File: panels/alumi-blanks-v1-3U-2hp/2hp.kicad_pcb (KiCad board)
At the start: 2 copper layers, 9.8 x 128.5 mm, 2 parts

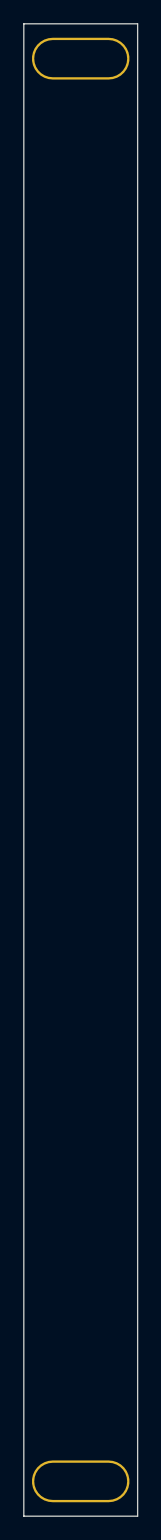
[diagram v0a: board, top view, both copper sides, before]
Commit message: feat: add new screw hole footprints and update panel KiCad files for new JLCPCB order
- Added modular-3M-screw-hole-size1-alumi-0604, modular-3M-screw-hole-size1-fit-alumi-0604, modular-3M-screw-hole-size2-alumi-0604
- Updated all panel .kicad_pcb and .kicad_pro files for 3U panels (1hp-16hp)
- Added new JLCPCB order snapshot and Gerber outputs

Co-authored-by: Copilot <223556219+Copilot@users.noreply.github.com>
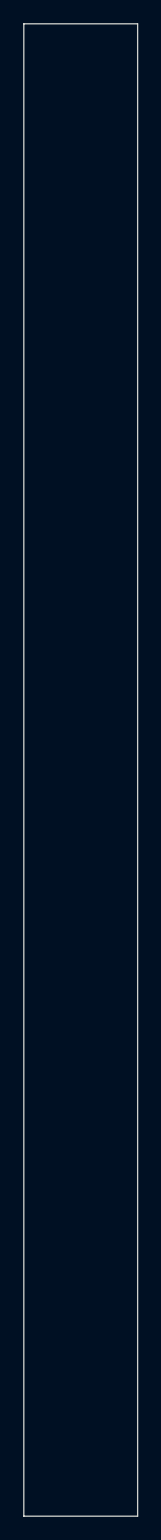
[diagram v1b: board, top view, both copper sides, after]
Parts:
- removed ?: , 
- removed the REF** at (4.90, 125.5)
- added REF**: modular-3M-screw-hole-size1-alumi-0604, zudo-blanks:modular-3M-screw-hole-size1-alumi-0604, F.Cu at (3.50, 3.00)
- added REF**: modular-3M-screw-hole-size1-alumi-0604, zudo-blanks:modular-3M-screw-hole-size1-alumi-0604, F.Cu at (6.29, 125.5)
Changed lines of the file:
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@@
 (kicad_pcb
-	(version 20240108)
+	(version 20260206)
 	(generator "pcbnew")
-	(generator_version "8.0")
+	(generator_version "10.0")
 	(general
 		(thickness 1.6)
@@
 	(layers
 		(0 "F.Cu" signal)
-		(31 "B.Cu" signal)
-		(32 "B.Adhes" user "B.Adhesive")
-		(33 "F.Adhes" user "F.Adhesive")
-		(34 "B.Paste" user)
-		(35 "F.Paste" user)
-		(36 "B.SilkS" user "B.Silkscreen")
-		(37 "F.SilkS" user "F.Silkscreen")
-		(38 "B.Mask" user)
-		(39 "F.Mask" user)
-		(40 "Dwgs.User" user "User.Drawings")
-		(41 "Cmts.User" user "User.Comments")
-		(42 "Eco1.User" user "User.Eco1")
-		(43 "Eco2.User" user "User.Eco2")
-		(44 "Edge.Cuts" user)
-		(45 "Margin" user)
-		(46 "B.CrtYd" user "B.Courtyard")
-		(47 "F.CrtYd" user "F.Courtyard")
-		(48 "B.Fab" user)
-		(49 "F.Fab" user)
-		(50 "User.1" user)
-		(51 "User.2" user)
-		(52 "User.3" user)
-		(53 "User.4" user)
-		(54 "User.5" user)
-		(55 "User.6" user)
-		(56 "User.7" user)
-		(57 "User.8" user)
-		(58 "User.9" user)
+		(2 "B.Cu" signal)
+		(9 "F.Adhes" user "F.Adhesive")
+		(11 "B.Adhes" user "B.Adhesive")
+		(13 "F.Paste" user)
+		(15 "B.Paste" user)
+		(5 "F.SilkS" user "F.Silkscreen")
+		(7 "B.SilkS" user "B.Silkscreen")
+		(1 "F.Mask" user)
+		(3 "B.Mask" user)
+		(17 "Dwgs.User" user "User.Drawings")
+		(19 "Cmts.User" user "User.Comments")
+		(21 "Eco1.User" user "User.Eco1")
+		(23 "Eco2.User" user "User.Eco2")
+		(25 "Edge.Cuts" user)
+		(27 "Margin" user)
+		(31 "F.CrtYd" user "F.Courtyard")
+		(29 "B.CrtYd" user "B.Courtyard")
+		(35 "F.Fab" user)
+		(33 "B.Fab" user)
+		(39 "User.1" user)
+		(41 "User.2" user)
+		(43 "User.3" user)
+		(45 "User.4" user)
+		(47 "User.5" user)
+		(49 "User.6" user)
+		(51 "User.7" user)
+		(53 "User.8" user)
+		(55 "User.9" user)
 	)
 	(setup
 		(pad_to_mask_clearance 0)
 		(allow_soldermask_bridges_in_footprints no)
+		(tenting
+			(front yes)
+			(back yes)
+		)
+		(covering
+			(front no)
+			(back no)
+		)
+		(plugging
+			(front no)
+			(back no)
+		)
+		(capping no)
+		(filling no)
 		(pcbplotparams
-			(layerselection 0x00010fc_ffffffff)
-			(plot_on_all_layers_selection 0x0000000_00000000)
+			(layerselection 0x00000000_00000000_55555555_5755555a)
+			(plot_on_all_layers_selection 0x00000000_00000000_00000000_00000000)
 			(disableapertmacros no)
 			(usegerberextensions no)
@@
 			(usegerberadvancedattributes yes)
 			(creategerberjobfile yes)
-			(dashed_line_dash_ratio 12.000000)
-			(dashed_line_gap_ratio 3.000000)
+			(dashed_line_dash_ratio 12)
+			(dashed_line_gap_ratio 3)
 			(svgprecision 4)
 			(plotframeref no)
-			(viasonmask no)
 			(mode 1)
 			(useauxorigin no)
-			(hpglpennumber 1)
-			(hpglpenspeed 20)
-			(hpglpendiameter 15.000000)
 			(pdf_front_fp_property_popups yes)
 			(pdf_back_fp_property_popups yes)
+			(pdf_metadata yes)
+			(pdf_single_document no)
 			(dxfpolygonmode yes)
 			(dxfimperialunits yes)
@@
 			(psnegative no)
 			(psa4output no)
-			(plotreference yes)
-			(plotvalue yes)
-			(plotfptext yes)
-			(plotinvisibletext no)
+			(plot_black_and_white yes)
 			(sketchpadsonfab no)
+			(plotpadnumbers no)
+			(hidednponfab no)
+			(sketchdnponfab yes)
+			(crossoutdnponfab yes)
 			(subtractmaskfromsilk no)
 			(outputformat 1)
@@
 		)
 	)
-	(net 0 "")
-	(footprint "Takazudo:M3-hole-little-wide-deco"
+	(footprint "zudo-blanks:modular-3M-screw-hole-size1-alumi-0604"
 		(layer "F.Cu")
-		(at 4.9 125.5)
+		(at 3.505 3)
 		(property "Reference" "REF**"
 			(at 0 -0.5 0)
@@
 			)
 		)
-		(property "Value" "M3-hole-little-wide-deco"
+		(property "Value" "modular-3M-screw-hole-size1-alumi-0604"
 			(at 0 1 0)
 			(unlocked yes)
@@
 			)
 		)
-		(property "Footprint" "Takazudo:M3-hole-little-wide-deco"
-			(at 0 0 0)
-			(unlocked yes)
-			(layer "F.Fab")
-			(hide yes)
-			(effects
-				(font
-					(size 1 1)
-					(thickness 0.15)
-				)
-			)
-		)
 		(property "Datasheet" ""
 			(at 0 0 0)
@@
 			)
 		)
-		(attr through_hole)
-		(pad "1" thru_hole roundrect
+		(attr smd)
+		(duplicate_pad_numbers_are_jumpers no)
+		(pad "" np_thru_hole roundrect
 			(at 0 0 90)
-			(size 3.6 8.4)
-			(drill oval 3.2 8)
-			(layers "*.Cu" "*.Mask")
-			(remove_unused_layers no)
-			(roundrect_rratio 0.5)
-		)
-	)
-	(footprint ""
+			(size 4 6)
+			(drill oval 3.2 5.2)
+			(layers "*.Mask")
+			(roundrect_rratio 0.4998750312)
+		)
+		(embedded_fonts no)
+	)
+	(footprint "zudo-blanks:modular-3M-screw-hole-size1-alumi-0604"
 		(layer "F.Cu")
-		(at 4.9 3)
-		(property "Reference" ""
-			(at 0 0 0)
+		(at 6.295 125.5)
+		(property "Reference" "REF**"
+			(at 0 -0.5 0)
+			(unlocked yes)
 			(layer "F.SilkS")
-			(effects
-				(font
-					(size 1.27 1.27)
-					(thickness 0.15)
-				)
-			)
-		)
-		(property "Value" ""
-			(at 0 0 0)
-			(layer "F.Fab")
-			(effects
-				(font
-					(size 1.27 1.27)
-					(thickness 0.15)
-				)
-			)
-		)
-		(property "Footprint" ""
-			(at 0 0 0)
-			(layer "F.Fab")
-			(hide yes)
-			(effects
-				(font
-					(size 1.27 1.27)
+			(hide yes)
+			(effects
+				(font
+					(size 1 1)
+					(thickness 0.1)
+				)
+			)
+		)
+		(property "Value" "modular-3M-screw-hole-size1-alumi-0604"
+			(at 0 1 0)
+			(unlocked yes)
+			(layer "F.Fab")
+			(hide yes)
+			(effects
+				(font
+					(size 1 1)
 					(thickness 0.15)
 				)
@@
 		(property "Datasheet" ""
 			(at 0 0 0)
-			(layer "F.Fab")
-			(hide yes)
-			(effects
-				(font
-					(size 1.27 1.27)
+			(unlocked yes)
+			(layer "F.Fab")
+			(hide yes)
+			(effects
+				(font
+					(size 1 1)
 					(thickness 0.15)
 				)
@@
 		(property "Description" ""
 			(at 0 0 0)
-			(layer "F.Fab")
-			(hide yes)
-			(effects
-				(font
-					(size 1.27 1.27)
-					(thickness 0.15)
-				)
-			)
-		)
-		(pad "1" thru_hole roundrect
+			(unlocked yes)
+			(layer "F.Fab")
+			(hide yes)
+			(effects
+				(font
+					(size 1 1)
+					(thickness 0.15)
+				)
+			)
+		)
+		(attr smd)
+		(duplicate_pad_numbers_are_jumpers no)
+		(pad "" np_thru_hole roundrect
 			(at 0 0 90)
-			(size 3.6 8.4)
-			(drill oval 3.2 8)
-			(layers "*.Cu" "*.Mask")
-			(remove_unused_layers no)
-			(roundrect_rratio 0.5)
-		)
+			(size 4 6)
+			(drill oval 3.2 5.2)
+			(layers "*.Mask")
+			(roundrect_rratio 0.4998750312)
+		)
+		(embedded_fonts no)
 	)
 	(gr_poly
@@
 			(type solid)
 		)
-		(fill solid)
+		(fill yes)
 		(layer "Edge.Cuts")
 	)
 	(gr_poly
 		(pts
+			(xy 0.69944 30.000381) (xy 0.000937 30.000381) (xy 0.000937 -0.000004) (xy 0.69944 -0.000004)
+		)
+		(stroke
+			(width -0.000001)
+			(type solid)
+		)
+		(fill yes)
+		(layer "User.1")
+	)
+	(gr_poly
+		(pts
+			(xy 4.901047 1.199447) (xy 0.000937 1.199447) (xy 0.000937 -0.000004) (xy 4.901047 -0.000004)
+		)
+		(stroke
+			(width -0.000001)
+			(type solid)
+		)
+		(fill yes)
+		(layer "User.1")
+	)
+	(gr_poly
+		(pts
 			(xy 9.797637 128.500015) (xy 9.099133 128.500015) (xy 9.099136 98.499626) (xy 9.79764 98.499626)
 		)
@@
 			(type solid)
 		)
-		(fill solid)
+		(fill yes)
 		(layer "User.1")
 	)
@@
 			(type solid)
 		)
-		(fill solid)
-		(layer "User.1")
-	)
-	(gr_poly
-		(pts
-			(xy 4.901047 1.199447) (xy 0.000937 1.199447) (xy 0.000937 -0.000004) (xy 4.901047 -0.000004)
-		)
-		(stroke
-			(width -0.000001)
-			(type solid)
-		)
-		(fill solid)
-		(layer "User.1")
-	)
-	(gr_poly
-		(pts
-			(xy 0.69944 30.000381) (xy 0.000937 30.000381) (xy 0.000937 -0.000004) (xy 0.69944 -0.000004)
-		)
-		(stroke
-			(width -0.000001)
-			(type solid)
-		)
-		(fill solid)
-		(layer "User.1")
-	)
+		(fill yes)
+		(layer "User.1")
+	)
+	(embedded_fonts no)
 )
